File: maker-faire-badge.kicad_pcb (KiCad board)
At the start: 2 copper layers, 101.6 x 18.8 mm, 38 parts, among them J1 USB-C, Q1 2N3906, Q2 2N3906, Q3 2N3906, Q4 2N3906, Q5 2N3906, Q6 2N3906

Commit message: User/ed cleanup (#2)
* Updated Library components

* Updated Silkscreen on Layout

* Added manufacturing files
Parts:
- BT1, BT2: value Battery_Cell -> ${REFERENCE}
- R1: value 59.2k -> 15.4k
- R10: value 40.2k -> 14k
- R12: value 14k -> 40.2k
- R3: value 15.4k -> 59.2k
- R4: value 48.7k -> 14.7k
- R6: value 14.7k -> 48.7k
- moved D2 22.2 mm to (159.0, 73.7)
- moved D4 22.2 mm to (150.4, 83.9)
- moved R16 22.2 mm to (135.9, 84.5)
- moved R17 22.2 mm to (159.0, 83.8)
- moved R9 22.2 mm to (135.9, 79.4)
- moved C1 22.2 mm to (99.1, 72.9)
- moved C2 22.2 mm to (99.1, 78.7)
- moved H1 22.2 mm to (104.1, 83.4)
- moved Q1 22.2 mm to (88.6, 72.9)
- moved Q2 22.2 mm to (88.6, 78.7)
- moved Q3 22.2 mm to (108.0, 72.9)
- moved Q4 22.2 mm to (108.0, 78.7)
- moved REF** 22.2 mm to (93.7, 84.1)
- moved C3 22.2 mm to (118.4, 72.9)
- moved C4 22.2 mm to (118.4, 78.7)
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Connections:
- net blue-led renamed LED-3
- net green-led renamed LED-2
- net red-led renamed LED-1
- C1 pad 1: base-2 -> BASE-1B
- C2 pad 1: base-1 -> BASE-1A
- C3 pad 1: base-4 -> BASE-2B
- C4 pad 1: base-3 -> BASE-2A
- C5 pad 1: base-6 -> BASE-3B
- C6 pad 1: base-5 -> BASE-3A
- Q1 pad 2: base-1 -> BASE-1A
- Q2 pad 2: base-2 -> BASE-1B
- Q3 pad 2: base-3 -> BASE-2A
- Q4 pad 2: base-4 -> BASE-2B
- Q5 pad 2: base-5 -> BASE-3A
- Q6 pad 2: base-6 -> BASE-3B
- R1 pad 1: base-2 -> GND
- R1 pad 2: GND -> BASE-1B
- R10 pad 1: base-6 -> GND
- R10 pad 2: GND -> BASE-3B
- R11 pad 1: Net-(Q5-C) -> GND
- R11 pad 2: GND -> Net-(Q5-C)
- R12 pad 1: base-5 -> GND
- R12 pad 2: GND -> BASE-3A
- R2 pad 1: Net-(Q1-C) -> GND
- R2 pad 2: GND -> Net-(Q1-C)
- R3 pad 1: base-1 -> GND
- R3 pad 2: GND -> BASE-1A
- R4 pad 1: base-4 -> GND
- R4 pad 2: GND -> BASE-2B
- R5 pad 1: Net-(Q3-C) -> GND
- R5 pad 2: GND -> Net-(Q3-C)
- R6 pad 1: base-3 -> GND
- R6 pad 2: GND -> BASE-2A
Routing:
- net base-6: track 22.9 -> 0.00 mm
- net BASE-1B: track 0.00 -> 22.9 mm
- net BASE-2B: track 0.00 -> 22.9 mm
- net base-4: track 22.9 -> 0.00 mm
- net base-2: track 22.9 -> 0.00 mm
- net BASE-3B: track 0.00 -> 22.9 mm
- net BASE-2A: track 0.00 -> 16.5 mm
- net base-5: track 16.5 -> 0.00 mm
- net base-3: track 16.5 -> 0.00 mm
- net BASE-1A: track 0.00 -> 16.5 mm
- net base-1: track 16.5 -> 0.00 mm
- net BASE-3A: track 0.00 -> 16.5 mm
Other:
- board text added: "1. Customer is to be contacted if one or more items listed below are in violation. 2. Design is a 2 layer board with a copper weight of 1 oz. 3. Board thickness is 1.6 mm 4. All trace widths are 6 mils or greater in the current design. 5. All trace clearances are 6 mils or greater in the current design. 6. PCB revision is on the bottom layer of copper as noted. Revision text is mirrored on this d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"
- board text added: "1. When possible, reference designators were placed within components. 2. 3 tables are included on the assembly drawing as follows: A. The component population that will set a color of D1 to either blink or stay solidly lit. B. The component population that will change the blink rate of a color of D1 when that color is set to blink. C. The component population that will set the power input config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"
- board text added: "ASSEMBLY NOTES"
- board text added: "BLINK LED 1"
- board text added: "BLINK LED 2"
- board text added: "BLINK LED 3"
- board text added: "DESIGNED BY 237 DECIMAL TO HEX"
- board text added: "LED SOLID BLINK 1 R15 R8 2 R14 R7 3 R16 R9"
- board text added: "LEDS 1,2,3 SOLID/BLINK"
- board text added: "REMOVE BATTERY BEFORE CONNECTING THE USB"
- board text added: "REV B"
- board text added: "Space for Manufacturer Markings on bottom side of board"
- board text added: "THE BATTERY OVERRIDES USB POWER"
- board text removed: "10.00 mils"
- board text removed: "2"
- board text removed: "4000.00 mils x 1090.00 mils"
- board text removed: "62.99 mils"
- board text removed: "7.00 mils / 7.00 mils"
- board text removed: "BLINK BLUE"
- board text removed: "BLINK GREEN"
- board text removed: "BLINK RED"
- board text removed: "BOARD CHARACTERISTICS"
- board text removed: "Board Thickness:"
- board text removed: "Board overall dimensions:"
- board text removed: "Castellated pads:"
- board text removed: "Copper Finish:"
- board text removed: "Copper Layer Count:"
- board text removed: "Edge card connectors:"
- board text removed: "HAL lead-free"
- board text removed: "Impedance Control:"
- board text removed: "Min hole diameter:"
- board text removed: "Min track/spacing:"
- board text removed: "NO BLINK LED R14 GREEN R15 RED R16 BLUE"
- board text removed: "No"
- board text removed: "Plated Board Edge:"
- board text removed: "REMOVE BATTERY BEFORE USING THE USB, THE BATTERY WILL DISCONNECT USB"
- board text removed: "REV A"

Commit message: updated design files
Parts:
- C1, C2, C3, C4, C5, C6: footprint Library:CP_Radial_D5.0mm_P2.50mm -> Capacitor_THT:CP_Radial_D5.0mm_P2.00mm
- D1: footprint Library:LED_D5.0mm-4_RGB_Wide_Pins -> LED_THT:LED_D5.0mm-4_RGB_Wide_Pins
- D2: footprint Library:D_DO-35_SOD27_P3.81mm_Vertical_KathodeUp -> Diode_THT:D_DO-35_SOD27_P3.81mm_Vertical_KathodeUp
- D3, D4: footprint Library:D_DO-201AD_P3.81mm_Vertical_KathodeUp -> Diode_THT:D_DO-201AD_P5.08mm_Vertical_KathodeUp
- H1: footprint Library:MountingHole_3.2mm_M3_Pad_Via -> MountingHole:MountingHole_3.2mm_M3_Pad_Via
- J1: footprint Library:USB_C_Receptacle_GCT_USB4125-xx-x-0190_6P_TopMnt_Horizontal -> Connector_USB:USB_C_Receptacle_GCT_USB4125-xx-x-0190_6P_TopMnt_Horizontal
- Q1, Q2, Q3, Q4, Q5, Q6: footprint Library:TO-92_Inline_Wide -> Package_TO_SOT_THT:TO-92_Inline_Wide
- R1, R10, R11, R12, R2, R3, R4, R5, R6, R7, R8, R9: footprint Library:R_Axial_DIN0207_L6.3mm_D2.5mm_P2.54mm_Vertical -> Resistor_THT:R_Axial_DIN0207_L6.3mm_D2.5mm_P2.54mm_Vertical
- R13, R17: footprint Library:R_Axial_DIN0207_L6.3mm_D2.5mm_P10.16mm_Horizontal -> Resistor_THT:R_Axial_DIN0207_L6.3mm_D2.5mm_P10.16mm_Horizontal
- R14, R15, R16: footprint Library:R_Axial_DIN0207_L6.3mm_D2.5mm_P7.62mm_Horizontal -> Resistor_THT:R_Axial_DIN0207_L6.3mm_D2.5mm_P7.62mm_Horizontal
- moved D4 1.02 mm to (149.4, 83.8)
- moved D3 0.91 mm to (145.5, 83.8)
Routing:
- net Net-(D3-K): track 23.7 -> 22.8 mm
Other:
- board text added: "REV C"
- board text added: "WayWayWay"
- board text removed: "BOTTOM LAYER"
- board text removed: "BOTTOM SILKSCREEN"
- board text removed: "BOTTOM SOLDERMASK"
- board text removed: "FABRICATION NOTES"
- board text removed: "TOP LAYER"
- board text removed: "TOP SILKSCREEN"
- board text removed: "TOP SOLDERMASK"

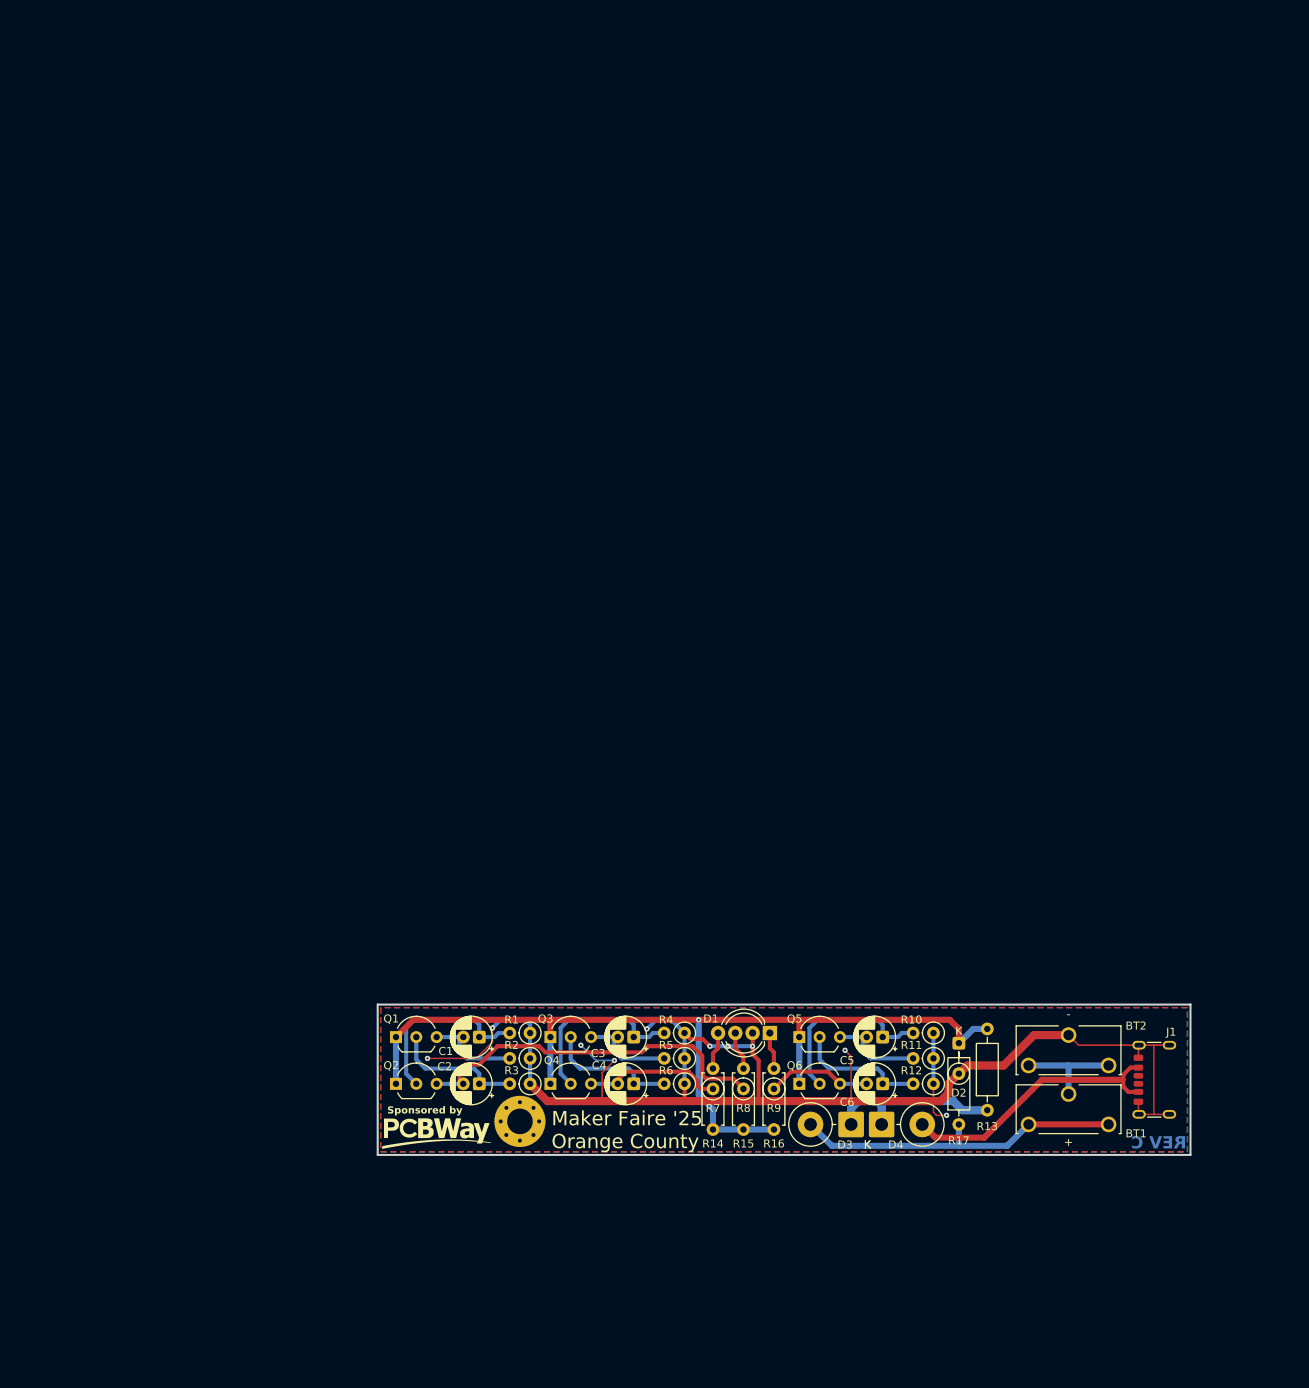
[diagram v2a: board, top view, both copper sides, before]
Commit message: Initial design if Acylic Display PCBA
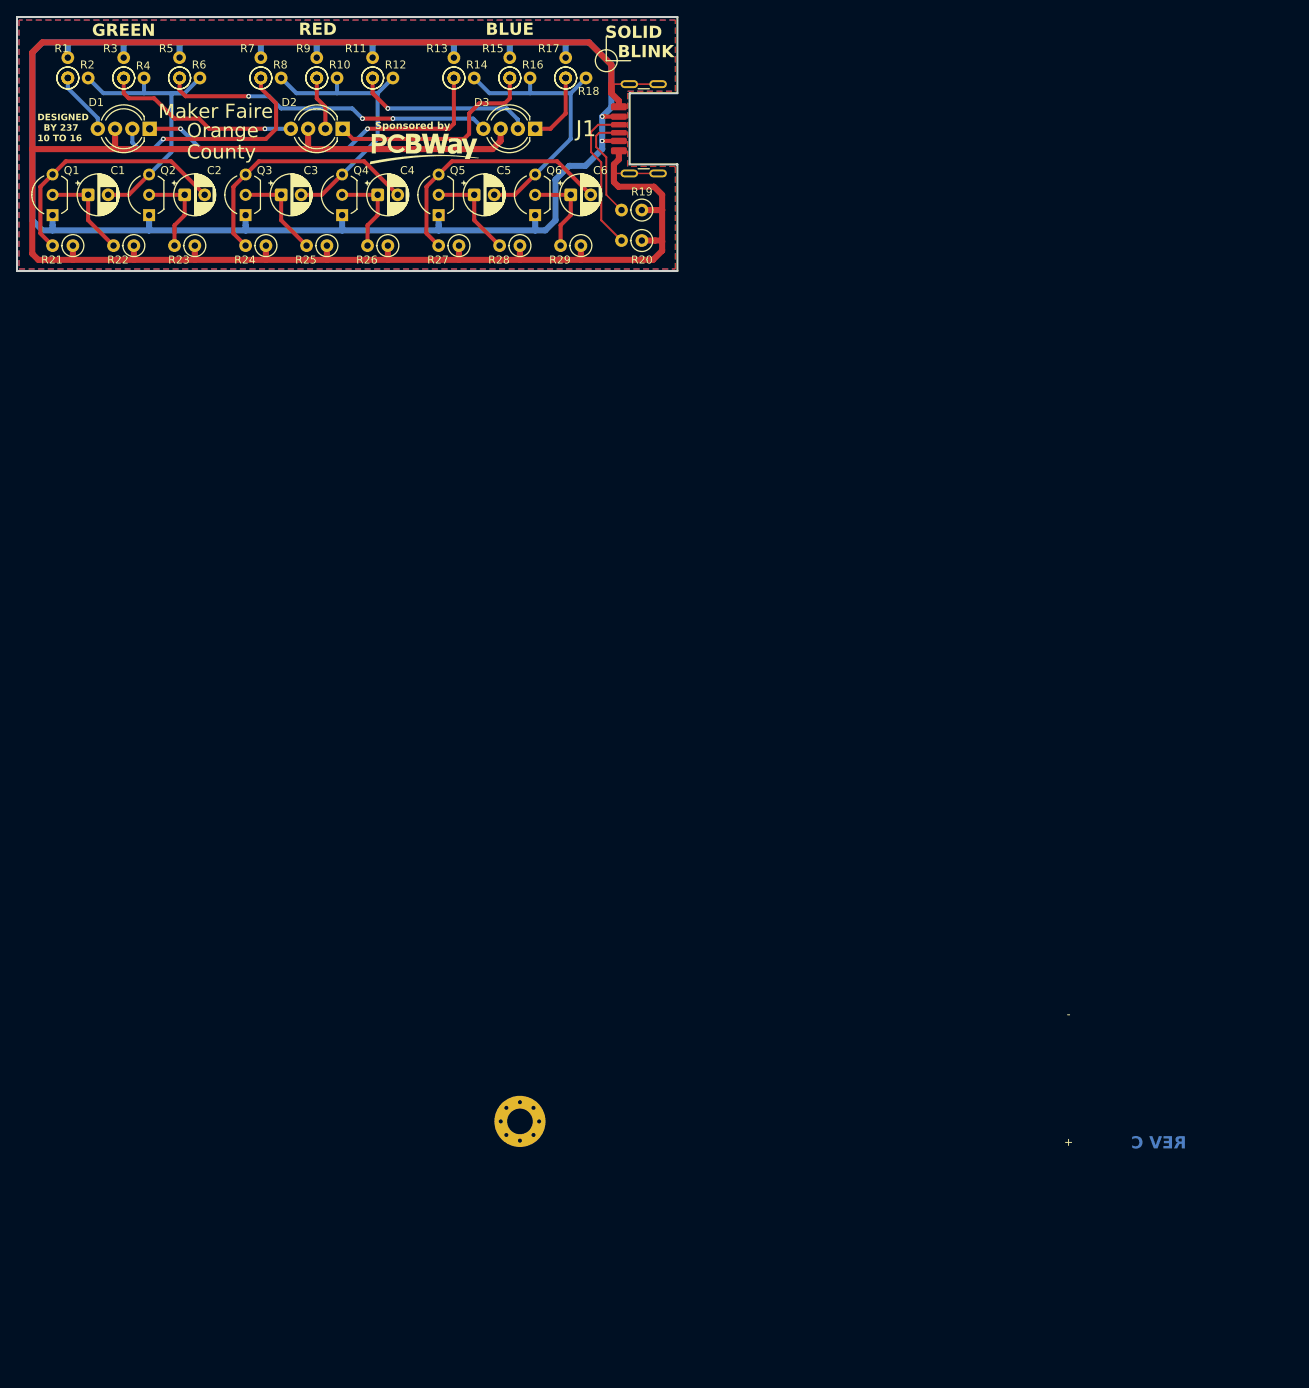
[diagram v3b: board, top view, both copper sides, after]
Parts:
- removed BT1, BT2: ${REFERENCE}, Library:BAT_1074
- removed the D3 at (145.5, 83.8)
- removed D4: 1N5822, Diode_THT:D_DO-201AD_P5.08mm_Vertical_KathodeUp
- removed the R17 at (159.0, 83.8)
- added D1: HV-5RGB60, LED_THT:LED_D5.0mm-4_RGB_Wide_Pins, F.Cu at (57.9, -40.6)
- added R1: 205, Resistor_THT:R_Axial_DIN0207_L6.3mm_D2.5mm_P2.54mm_Vertical, F.Cu at (47.6, -47.0)
- added R10: 95.3, Resistor_THT:R_Axial_DIN0207_L6.3mm_D2.5mm_P2.54mm_Vertical, F.Cu at (78.7, -47.0)
- added R14: 95.3, Resistor_THT:R_Axial_DIN0207_L6.3mm_D2.5mm_P2.54mm_Vertical, F.Cu at (95.9, -47.0)
- added R15: 205, Resistor_THT:R_Axial_DIN0207_L6.3mm_D2.5mm_P2.54mm_Vertical, F.Cu at (102.9, -47.0)
- added R16: 95.3, Resistor_THT:R_Axial_DIN0207_L6.3mm_D2.5mm_P2.54mm_Vertical, F.Cu at (102.9, -47.0)
- added R19: 5.1k, Resistor_THT:R_Axial_DIN0207_L6.3mm_D2.5mm_P2.54mm_Vertical, F.Cu at (119.4, -30.5)
- added R2: 95.3, Resistor_THT:R_Axial_DIN0207_L6.3mm_D2.5mm_P2.54mm_Vertical, F.Cu at (47.6, -47.0)
- added R20: 5.1k, Resistor_THT:R_Axial_DIN0207_L6.3mm_D2.5mm_P2.54mm_Vertical, F.Cu at (119.4, -26.7)
- added R3: 205, Resistor_THT:R_Axial_DIN0207_L6.3mm_D2.5mm_P2.54mm_Vertical, F.Cu at (54.6, -47.0)
- added R4: 95.3, Resistor_THT:R_Axial_DIN0207_L6.3mm_D2.5mm_P2.54mm_Vertical, F.Cu at (54.6, -47.0)
- added R7: 205, Resistor_THT:R_Axial_DIN0207_L6.3mm_D2.5mm_P2.54mm_Vertical, F.Cu at (71.8, -47.0)
- added R8: 95.3, Resistor_THT:R_Axial_DIN0207_L6.3mm_D2.5mm_P2.54mm_Vertical, F.Cu at (71.8, -47.0)
- added R9: 205, Resistor_THT:R_Axial_DIN0207_L6.3mm_D2.5mm_P2.54mm_Vertical, F.Cu at (78.7, -47.0)
- C1: renamed from C4; footprint Capacitor_THT:CP_Radial_D5.0mm_P2.00mm -> Capacitor_THT:CP_Radial_D5.0mm_P2.50mm
- C2: renamed from C3; footprint Capacitor_THT:CP_Radial_D5.0mm_P2.00mm -> Capacitor_THT:CP_Radial_D5.0mm_P2.50mm
- C3: renamed from C2; footprint Capacitor_THT:CP_Radial_D5.0mm_P2.00mm -> Capacitor_THT:CP_Radial_D5.0mm_P2.50mm
- C4: renamed from C1; footprint Capacitor_THT:CP_Radial_D5.0mm_P2.00mm -> Capacitor_THT:CP_Radial_D5.0mm_P2.50mm
- C5: renamed from C6; footprint Capacitor_THT:CP_Radial_D5.0mm_P2.00mm -> Capacitor_THT:CP_Radial_D5.0mm_P2.50mm
- C6: renamed from C5; footprint Capacitor_THT:CP_Radial_D5.0mm_P2.00mm -> Capacitor_THT:CP_Radial_D5.0mm_P2.50mm
- D2: value 3V9 -> HV-5RGB60; footprint Diode_THT:D_DO-35_SOD27_P3.81mm_Vertical_KathodeUp -> LED_THT:LED_D5.0mm-4_RGB_Wide_Pins
- J1: footprint Connector_USB:USB_C_Receptacle_GCT_USB4125-xx-x-0190_6P_TopMnt_Horizontal -> Connector_USB:USB_C_Receptacle_GCT_USB4135-GF-A_6P_TopMnt_Horizontal
- R11: renamed from R15; footprint Resistor_THT:R_Axial_DIN0207_L6.3mm_D2.5mm_P7.62mm_Horizontal -> Resistor_THT:R_Axial_DIN0207_L6.3mm_D2.5mm_P2.54mm_Vertical
- R13: value 20.5 -> 205; footprint Resistor_THT:R_Axial_DIN0207_L6.3mm_D2.5mm_P10.16mm_Horizontal -> Resistor_THT:R_Axial_DIN0207_L6.3mm_D2.5mm_P2.54mm_Vertical
- R17: renamed from R16; footprint Resistor_THT:R_Axial_DIN0207_L6.3mm_D2.5mm_P7.62mm_Horizontal -> Resistor_THT:R_Axial_DIN0207_L6.3mm_D2.5mm_P2.54mm_Vertical
- R21: renamed from R5; value 205 -> 261
- R22: renamed from R6; value 48.7k -> 82k
- R23: renamed from R4; value 14.7k -> 30k
- R24: renamed from R2; value 205 -> 261
- R25: renamed from R3; value 59.2k -> 150k
- R26: renamed from R1; value 15.4k -> 30k
- R27: renamed from R11; value 205 -> 261
- R28: renamed from R12; value 40.2k -> 110k
- R29: renamed from R10; value 14k -> 30k
- R5: renamed from R14; footprint Resistor_THT:R_Axial_DIN0207_L6.3mm_D2.5mm_P7.62mm_Horizontal -> Resistor_THT:R_Axial_DIN0207_L6.3mm_D2.5mm_P2.54mm_Vertical
- moved R5 147.4 mm to (61.6, -47.0)
- moved R13 145.2 mm to (95.9, -47.0)
- moved R6 142.9 mm to (61.6, -47.0), turned to 0 degrees
- moved R11 139.4 mm to (85.7, -47.0)
- moved D2 137.8 mm to (82.0, -40.6), turned to 180 degrees
- moved R12 134.6 mm to (85.7, -47.0), turned to 0 degrees
- moved J1 134.6 mm to (121.4, -40.6)
- moved R17 134.0 mm to (109.9, -47.0)
- moved C1 130.4 mm to (50.2, -32.4), turned to 0 degrees
- moved R18 129.0 mm to (109.9, -47.0), turned to 0 degrees
- moved R21 127.2 mm to (48.3, -26.0)
- moved R22 125.4 mm to (55.9, -26.0)
- moved REF** 123.1 mm to (92.2, -39.0)
- moved C5 122.3 mm to (98.4, -32.4), turned to 0 degrees
- moved Q1 120.1 mm to (45.7, -29.8), turned to 90 degrees
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- renumbered D1 to D3, Q3 to Q1, Q4 to Q2, Q1 to Q3, Q2 to Q4, R8 to R12, R9 to R18, R7 to R6
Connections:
- C1 pad 2: Net-(Q4-C) -> LED-2
- C3 pad 2: Net-(Q2-C) -> LED-1
- C5 pad 2: Net-(Q6-C) -> LED-3
- D2 pad 1: Vcc -> Net-(D2-BA)
- D2 pad 2: GND -> Net-(D2-RA)
- D3 pad 1: LED-3 -> Net-(D3-BA)
- D3 pad 2: GND -> Net-(D3-RA)
- D3 pad 3: LED-1 -> GND
- D3 pad 4: LED-2 -> Net-(D3-GA)
- J1 pad A5: unconnected-(J1-CC1-PadA5) -> Net-(J1-CC1)
- J1 pad A9: Net-(D4-A) -> Vcc
- J1 pad B5: unconnected-(J1-CC2-PadB5) -> Net-(J1-CC2)
- J1 pad B9: Net-(D4-A) -> Vcc
- Q2 pad 3: Net-(Q4-C) -> LED-2
- Q4 pad 3: Net-(Q2-C) -> LED-1
- Q6 pad 3: Net-(Q6-C) -> LED-3
- R11 pad 1: Vcc -> Net-(D3-RA)
- R11 pad 2: LED-1 -> Vcc
- R12 pad 1: Net-(Q2-C) -> Net-(D3-RA)
- R17 pad 1: Vcc -> Net-(D3-BA)
- R17 pad 2: LED-3 -> Vcc
- R18 pad 1: Net-(Q6-C) -> Net-(D3-BA)
- R5 pad 1: Vcc -> Net-(D3-GA)
- R5 pad 2: LED-2 -> Vcc
- R6 pad 1: Net-(Q4-C) -> Net-(D3-GA)
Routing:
- net GND: track 186.1 -> 301.4 mm, vias 10 -> 0
- net Vcc: track 121.7 -> 217.7 mm, vias 1 -> 2
- net Net-(Q2-C): track 45.5 -> 0.00 mm
- net Net-(BT1-+): track 42.1 -> 0.00 mm
- net Net-(D3-GA): track 0.00 -> 41.5 mm, vias 0 -> 3
- net Net-(D4-A): track 34.6 -> 0.00 mm
- net LED-2: track 4.71 -> 36.6 mm
- net LED-3: track 4.66 -> 35.6 mm
- net LED-1: track 4.87 -> 35.6 mm
- net Net-(D1-RA): track 0.00 -> 28.2 mm, vias 0 -> 1
- net Net-(D2-BA): track 0.00 -> 27.5 mm
- net Net-(D2-GA): track 0.00 -> 24.6 mm, vias 0 -> 1
- net Net-(D1-BA): track 22.8 -> 46.1 mm, vias 0 -> 2
- net Net-(D3-RA): track 0.00 -> 22.6 mm, vias 0 -> 1
- net Net-(Q5-C): track 11.2 -> 31.6 mm
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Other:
- board size 101.6 x 18.8 mm -> 82.6 x 31.8 mm
- board text added: "BLINK"
- board text added: "BLUE"
- board text added: "County"
- board text added: "DESIGNED BY 237 10 TO 16"
- board text added: "GREEN"
- board text added: "Maker Faire"
- board text added: "Orange"
- board text added: "RED"
- board text added: "SOLID"
- board text removed: "DESIGNED BY 237 DECIMAL TO HEX"
